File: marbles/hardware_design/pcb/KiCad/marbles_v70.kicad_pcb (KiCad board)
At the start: 2 copper layers, 88.9 x 106 mm, 213 parts, among them IC1 R-78E3.3-0.5, IC10 TL074PW, IC2 STM32F405RGT6, IC3 LD2981ABU33, IC4 DAC8164ICPW, IC5 MCP6004, IC6 MCP6004, IC7 OPA4171, IC8 LM4040B10, IC9 LM324PW, J1 PJ301_THONKICONN6, J10 PJ301_THONKICONN6, J11 PJ301_THONKICONN6, J12 PJ301_THONKICONN6, J13 PJ301_THONKICONN6, J14 PJ301_THONKICONN6, J15 PJ301_THONKICONN6, J16 PJ301_THONKICONN6, J2 PJ301_THONKICONN6, J3 PJ301_THONKICONN6, J4 PJ301_THONKICONN6, J5 PJ301_THONKICONN6, J6 PJ301_THONKICONN6, J7 PJ301_THONKICONN6, J8 PJ301_THONKICONN6, J9 PJ301_THONKICONN6, Q1 8MHz, Q2 MMBT3904, Q3 MMBT3904, SW1 LP4OA1PBCT, SW2 LP4OA1PBCT, SW3 TAC_SWITCHPTH, SW4 TAC_SWITCHPTH, SW5 TAC_SWITCHPTH, SW6 TAC_SWITCHPTH, SW7 TAC_SWITCHPTH

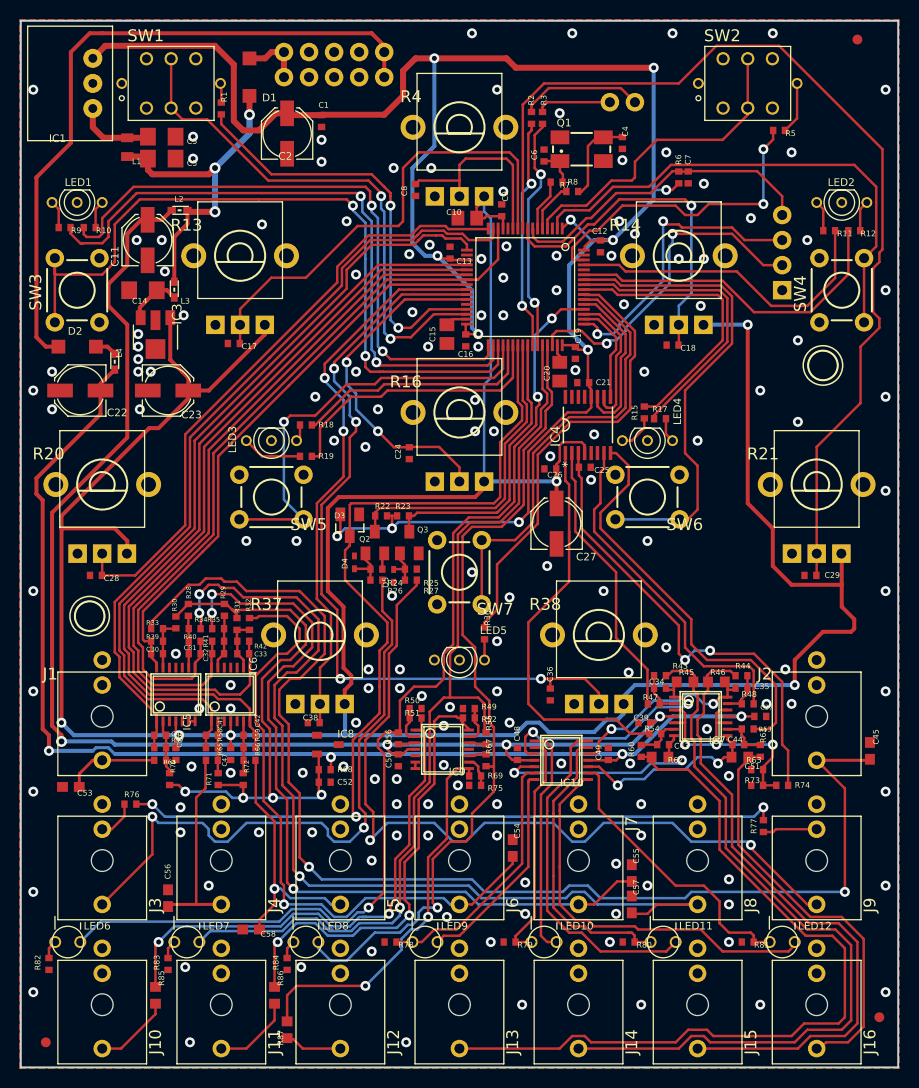
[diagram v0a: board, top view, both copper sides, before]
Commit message: Marbles added
Beware! T_clock is shorted to ground. Fix before using this PCB
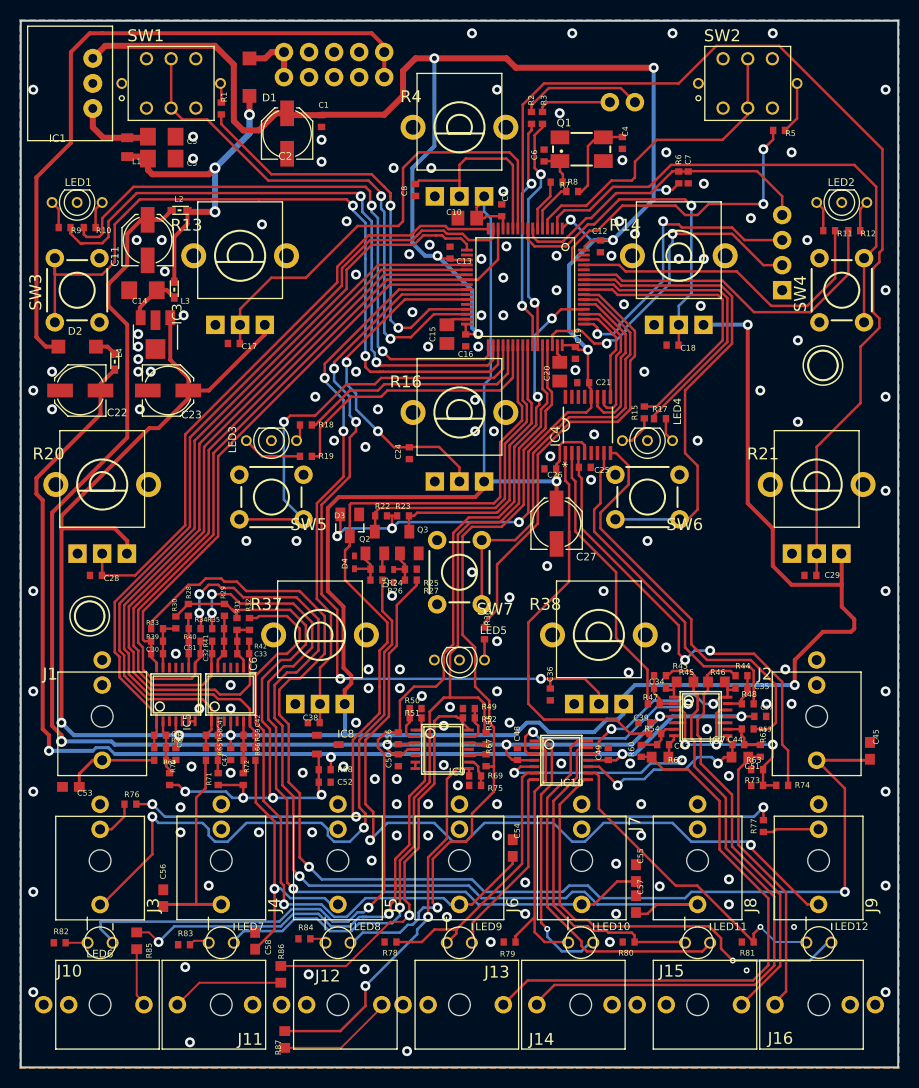
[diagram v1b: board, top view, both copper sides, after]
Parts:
- removed F1, F2: FIDUCIAL1X2, marbles_v70:FIDUCIAL-1X2
- removed U$2: , marbles_v70:ROHS_BIG
- removed U$4: , marbles_v70:CE_MEDIUM
- removed U$5: , marbles_v70:FCC_MEDIUM
- moved R85 5.84 mm to (115.8, 145.2)
- moved LED10 3.72 mm to (160.8, 145.4)
- moved LED12 3.71 mm to (184.9, 145.4)
- moved LED11 3.49 mm to (172.6, 145.4)
- moved LED7 3.49 mm to (124.4, 145.4)
- moved LED9 3.48 mm to (148.5, 145.4)
- moved LED6 3.28 mm to (112.1, 145.4)
- moved LED8 3.25 mm to (136.2, 145.4)
- moved R84 3.09 mm to (132.8, 145.0), turned to 0 degrees
- moved R83 2.54 mm to (120.6, 145.6), turned to 0 degrees
- moved R82 2.41 mm to (108.0, 145.4), turned to 0 degrees
- moved R86 2.22 mm to (130.4, 148.6)
- moved C58 1.22 mm to (127.8, 145.2), turned to 90 degrees
- moved R87 1.01 mm to (130.8, 155.2)
- moved C56 0.48 mm to (118.5, 140.9)
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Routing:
- net Net-(J13-PadP3): track 80.3 -> 57.0 mm
- net Net-(J15-PadP3): track 65.4 -> 42.2 mm
- net Net-(J14-PadP3): track 76.4 -> 62.5 mm
- net Net-(J16-PadP3): track 41.8 -> 29.3 mm
- net Net-(J12-PadP3): track 5.83 -> 11.9 mm
- net GATE_T_3: track 84.3 -> 79.0 mm
- net Net-(IC9-Pad14): track 46.0 -> 40.9 mm, vias 2 -> 1
- net Net-(IC10-Pad8): track 40.4 -> 45.0 mm, vias 0 -> 1
- net Net-(IC10-Pad1): track 23.4 -> 27.3 mm, vias 0 -> 1
- net Net-(IC10-Pad14): track 34.7 -> 38.4 mm
- net GATE_T_2: track 95.5 -> 91.9 mm
- net Net-(IC10-Pad13): track 29.8 -> 33.3 mm
- net Net-(IC10-Pad2): track 23.5 -> 27.0 mm
- net Net-(IC10-Pad9): track 29.1 -> 32.6 mm, vias 0 -> 1
- net Net-(J11-PadP3): track 8.49 -> 11.4 mm
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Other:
- net class Default removed
- board text added: "2025. v8"
- board text added: "Pebbles"
- board text removed: "2017. v7"
- board text removed: "Marbles"
